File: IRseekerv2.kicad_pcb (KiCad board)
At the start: 2 copper layers, 80 x 80 mm, 49 parts, among them J13 Conn_01x04_Pin, J14 Conn_01x02_Pin, J15 SEL_VOLTAGE, J16 G, J17 G, J18 G, J19 G, J20 Conn_01x02_Pin, J26 Conn_01x02_Pin, J27 Conn_01x02_Pin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

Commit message: BOOT0 pulldown instead of pullup
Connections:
- R3 pad 1: +3.3V -> GND
- SW2 pad 2: GND -> +3.3V
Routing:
- net GND: track 44.2 -> 54.6 mm, vias 26 -> 28
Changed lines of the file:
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@@
       (net 16 "BOOT0") (pinfunction "1") (pintype "passive"))
     (pad "2" thru_hole circle (at 0 4.5 270) (size 2 2) (drill 1.1) (layers "*.Cu" "*.Mask")
-      (net 4 "GND") (pinfunction "2") (pintype "passive"))
+      (net 5 "+3.3V") (pinfunction "2") (pintype "passive"))
     (pad "2" thru_hole circle (at 6.5 4.5 270) (size 2 2) (drill 1.1) (layers "*.Cu" "*.Mask")
-      (net 4 "GND") (pinfunction "2") (pintype "passive"))
+      (net 5 "+3.3V") (pinfunction "2") (pintype "passive"))
     (model "${KICAD6_3DMODEL_DIR}/Button_Switch_THT.3dshapes/SW_PUSH_6mm.wrl"
       (offset (xyz 0 0 0))
@@
       (stroke (width 0.1) (type solid)) (layer "F.Fab"))
     (pad "1" smd roundrect (at -0.825 0) (size 0.8 0.95) (layers "F.Cu" "F.Paste" "F.Mask") (roundrect_rratio 0.25)
-      (net 5 "+3.3V") (pintype "passive"))
+      (net 4 "GND") (pintype "passive"))
     (pad "2" smd roundrect (at 0.825 0) (size 0.8 0.95) (layers "F.Cu" "F.Paste" "F.Mask") (roundrect_rratio 0.25)
       (net 16 "BOOT0") (pintype "passive"))
@@
     (effects (font (size 0.75 0.75) (thickness 0.1875) bold) (justify left bottom mirror))
   )
+  (gr_text "5V" (at 105.89 125.15) (layer "B.SilkS")
+    (effects (font (size 0.75 0.75) (thickness 0.1875) bold) (justify left bottom mirror))
+  )
   (gr_text "TX_3V" (at 119.96 100.614 90) (layer "B.SilkS")
     (effects (font (size 0.75 0.75) (thickness 0.1875) bold) (justify left bottom mirror))
   )
+  (gr_text "GND" (at 108.74 125.2) (layer "B.SilkS")
+    (effects (font (size 0.75 0.75) (thickness 0.1875) bold) (justify left bottom mirror))
+  )
   (gr_text "3V" (at 134.826 109.088 90) (layer "B.SilkS")
     (effects (font (size 0.75 0.75) (thickness 0.1875) bold) (justify left bottom mirror))
@@
     (effects (font (size 0.75 0.75) (thickness 0.1875) bold) (justify left bottom))
   )
-  (gr_text "5V" (at 106.7 123.9 90) (layer "F.SilkS")
+  (gr_text "5V" (at 104.32 125.14) (layer "F.SilkS")
     (effects (font (size 0.75 0.75) (thickness 0.1875) bold) (justify left bottom))
   )
@@
     (effects (font (size 1.5 1.5) (thickness 0.3)))
   )
-  (gr_text "GND" (at 106.65 127.25 90) (layer "F.SilkS")
+  (gr_text "GND" (at 106.27 125.2) (layer "F.SilkS")
     (effects (font (size 0.75 0.75) (thickness 0.1875) bold) (justify left bottom))
   )
@@
   (segment (start 106.335 109.64) (end 106.35 109.655) (width 0.25) (layer "F.Cu") (net 4))
   (segment (start 106.35 109.655) (end 108.35 109.655) (width 0.25) (layer "F.Cu") (net 4))
+  (segment (start 90.265 75.17) (end 89.9 75.17) (width 0.25) (layer "F.Cu") (net 4))
   (segment (start 103.7298 82.3805) (end 105.6525 82.3805) (width 0.25) (layer "F.Cu") (net 4))
+  (segment (start 89.32 82.135) (end 91.03 80.425) (width 0.25) (layer "F.Cu") (net 4))
   (segment (start 103.06 109.64) (end 104.5311 109.64) (width 0.25) (layer "F.Cu") (net 4))
   (segment (start 100.2401 90.5964) (end 101.2964 90.5964) (width 0.25) (layer "F.Cu") (net 4))
   (segment (start 104.5311 109.64) (end 104.5311 109.418) (width 0.25) (layer "F.Cu") (net 4))
+  (segment (start 89.32 82.22) (end 89.32 82.135) (width 0.25) (layer "F.Cu") (net 4))
   (segment (start 111.6919 123.1652) (end 113.48 124.9533) (width 0.25) (layer "F.Cu") (net 4))
   (segment (start 77.395 98.91) (end 77.395 97.74) (width 0.25) (layer "F.Cu") (net 4))
@@
   (segment (start 114.7293 97.8136) (end 113.8814 97.8136) (width 0.25) (layer "F.Cu") (net 4))
   (segment (start 115.7734 73.1094) (end 116.6236 73.1094) (width 0.25) (layer "F.Cu") (net 4))
+  (segment (start 89.9 75.17) (end 88.94 76.13) (width 0.25) (layer "F.Cu") (net 4))
   (segment (start 94.9076 97.3126) (end 95.275 97.68) (width 0.25) (layer "F.Cu") (net 4))
   (segment (start 108.35 109.655) (end 108.36 109.665) (width 0.25) (layer "F.Cu") (net 4))
@@
   (via (at 103.06 100.54) (size 0.8) (drill 0.4) (layers "F.Cu" "B.Cu") (net 4))
   (via (at 103.56 99.54) (size 0.8) (drill 0.4) (layers "F.Cu" "B.Cu") (net 4))
+  (via (at 89.32 82.22) (size 0.8) (drill 0.4) (layers "F.Cu" "B.Cu") (net 4))
   (via (at 102.13 99.5) (size 0.8) (drill 0.4) (layers "F.Cu" "B.Cu") (net 4))
   (via (at 106.23 100.46) (size 0.8) (drill 0.4) (layers "F.Cu" "B.Cu") (net 4))
@@
   (via (at 115.7734 73.1094) (size 0.8) (drill 0.4) (layers "F.Cu" "B.Cu") (net 4))
   (via (at 87.8748 91.9783) (size 0.8) (drill 0.4) (layers "F.Cu" "B.Cu") (net 4))
+  (via (at 88.94 76.13) (size 0.8) (drill 0.4) (layers "F.Cu" "B.Cu") (net 4))
   (via (at 104.92 98.42) (size 0.8) (drill 0.4) (layers "F.Cu" "B.Cu") (net 4))
   (via (at 103.95 100.52) (size 0.8) (drill 0.4) (layers "F.Cu" "B.Cu") (net 4))
   (via (at 100.2401 90.5964) (size 0.8) (drill 0.4) (layers "F.Cu" "B.Cu") (net 4))
   (via (at 92.1279 80.4589) (size 0.8) (drill 0.4) (layers "F.Cu" "B.Cu") (net 4))
+  (segment (start 89.32 76.51) (end 89.32 82.22) (width 0.25) (layer "B.Cu") (net 4))
   (segment (start 93.5333 98.132195) (end 97.400255 101.99915) (width 0.25) (layer "B.Cu") (net 4))
   (segment (start 100.61085 101.99915) (end 102.13 100.48) (width 0.25) (layer "B.Cu") (net 4))
   (segment (start 102.14 99.51) (end 102.13 99.5) (width 3) (layer "B.Cu") (net 4))
   (segment (start 106.23 99.51) (end 102.14 99.51) (width 3) (layer "B.Cu") (net 4))
+  (segment (start 88.94 76.13) (end 89.32 76.51) (width 0.25) (layer "B.Cu") (net 4))
   (segment (start 97.400255 101.99915) (end 100.61085 101.99915) (width 0.25) (layer "B.Cu") (net 4))
   (segment (start 93.5333 97.3126) (end 93.5333 98.132195) (width 0.25) (layer "B.Cu") (net 4))
@@
     (polygon
       (pts
-        (xy 197.75 176.25)
-        (xy -8.75 178)
-        (xy -9.5 18.75)
-        (xy 197.75 18.75)
+        (xy 167.06 153.7)
+        (xy 47.24 152.48)
+        (xy 49.27 48.1)
+        (xy 167.87 47.69)
       )
     )
@@
     (polygon
       (pts
-        (xy 194 -4)
-        (xy 189.5 226.25)
-        (xy 15.75 231.25)
-        (xy 14 -8)
+        (xy 163 55.81)
+        (xy 162.59 150.04)
+        (xy 51.3 148.82)
+        (xy 52.12 55.81)
       )
     )

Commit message: Added label for site and "designed by"
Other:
- board text added: "Designed by Marek Maszay https://github.com/markosko/IRseeker-kicad"
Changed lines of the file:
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@@
   (gr_circle (center 104.09 100.4) (end 144.09 100.4)
     (stroke (width 0.2) (type solid)) (fill none) (layer "Edge.Cuts"))
+  (gr_text "Designed by\nMarek Maszay\nhttps://github.com/markosko/IRseeker-kicad" (at 103.41 98.6) (layer "B.SilkS")
+    (effects (font (size 1 1) (thickness 0.25) bold) (justify bottom mirror))
+  )
   (gr_text "3V" (at 120.04 108.97 90) (layer "B.SilkS")
     (effects (font (size 0.75 0.75) (thickness 0.1875) bold) (justify left bottom mirror))

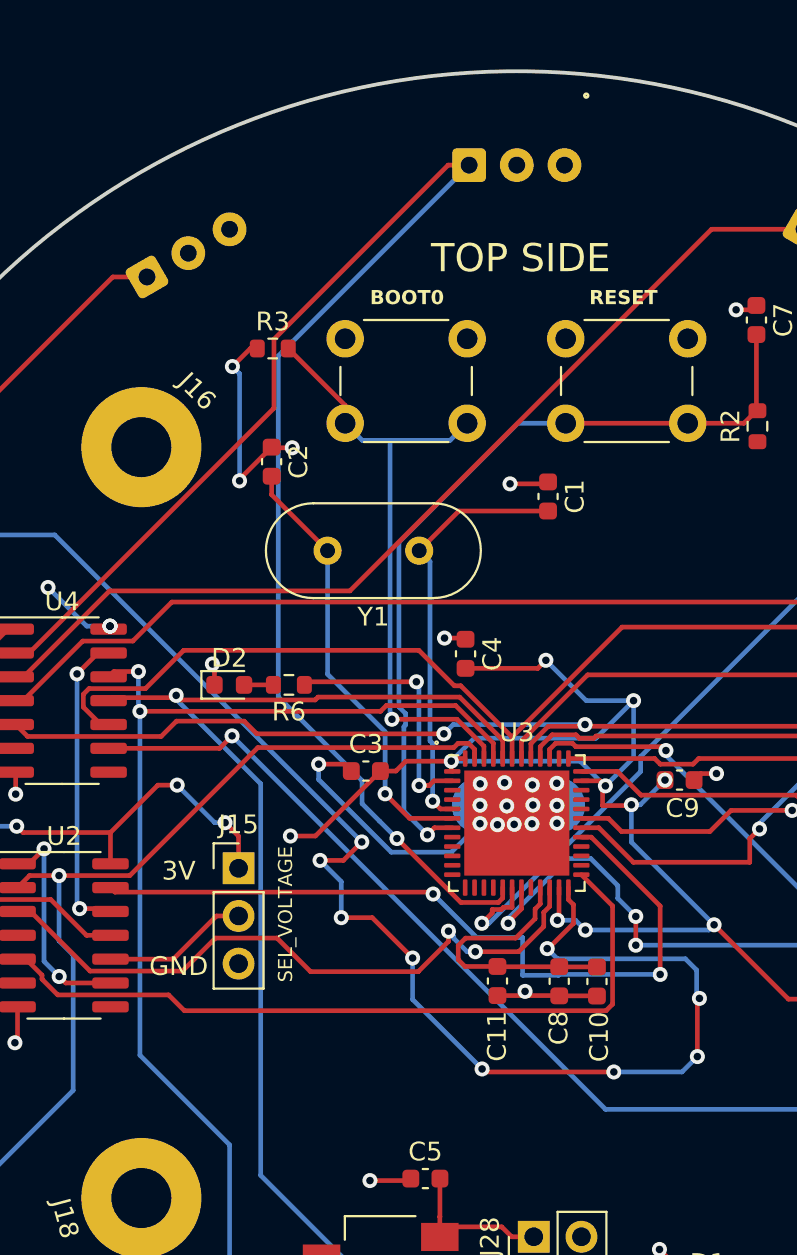
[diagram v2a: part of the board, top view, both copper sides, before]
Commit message: removed SEL_VOlTAGE and added OUTGATE pin out
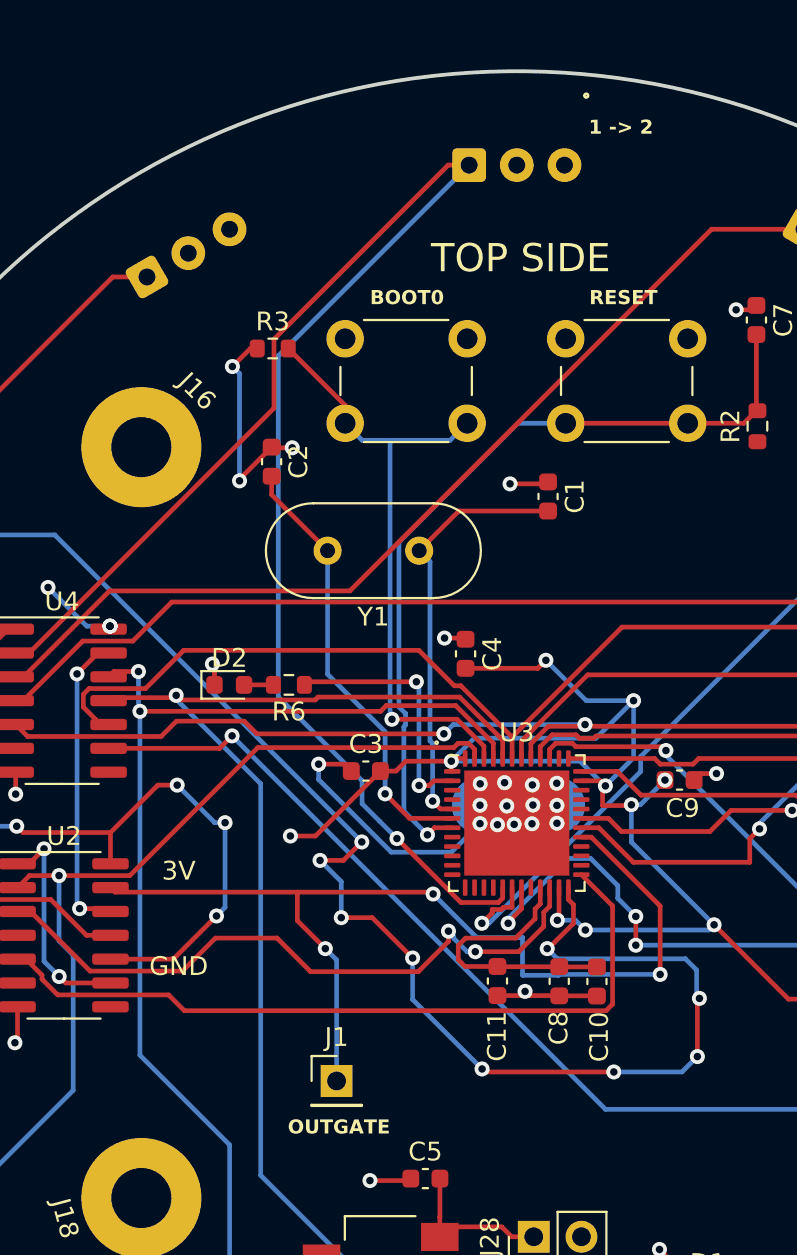
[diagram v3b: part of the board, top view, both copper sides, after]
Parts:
- removed J15: SEL_VOLTAGE, Connector_PinHeader_2.54mm:PinHeader_1x03_P2.54mm_Vertical
- added J1: Conn_01x01_Pin, Connector_PinHeader_2.54mm:PinHeader_1x01_P2.54mm_Vertical, F.Cu at (94.5, 114.2)
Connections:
- U2 pad 10: Net-(J15-Pin_2) -> +3.3V
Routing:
- net OUT_GATE: track 41.8 -> 52.7 mm, vias 2 -> 3
- net +3.3V: track 130.5 -> 139.6 mm, vias 19 -> 20
- net Net-(J15-Pin_2): track 7.78 -> 0.00 mm
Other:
- board text added: "1 -> 2"
- board text added: "2 <- 1"
- board text added: "BOTTOM SIDE"
- board text added: "OUTGATE"

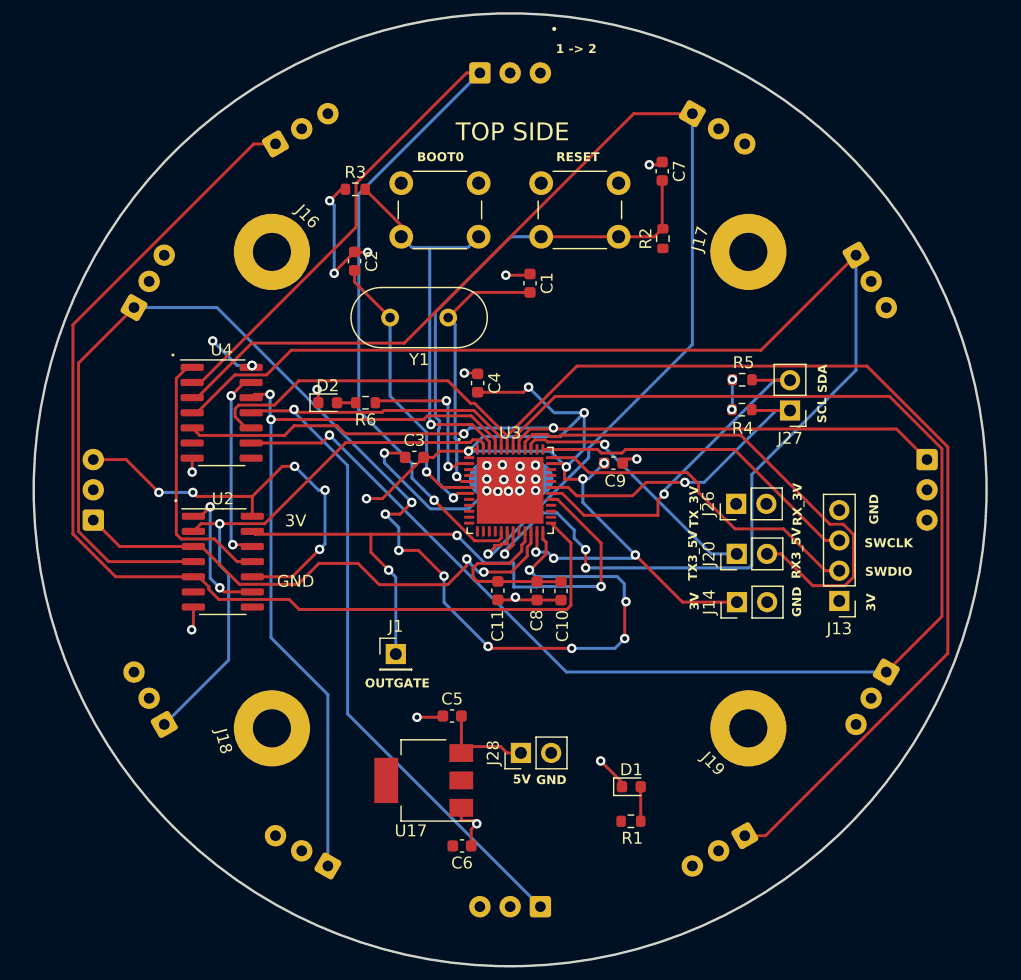
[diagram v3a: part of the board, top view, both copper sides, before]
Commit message: change crystal to smd version
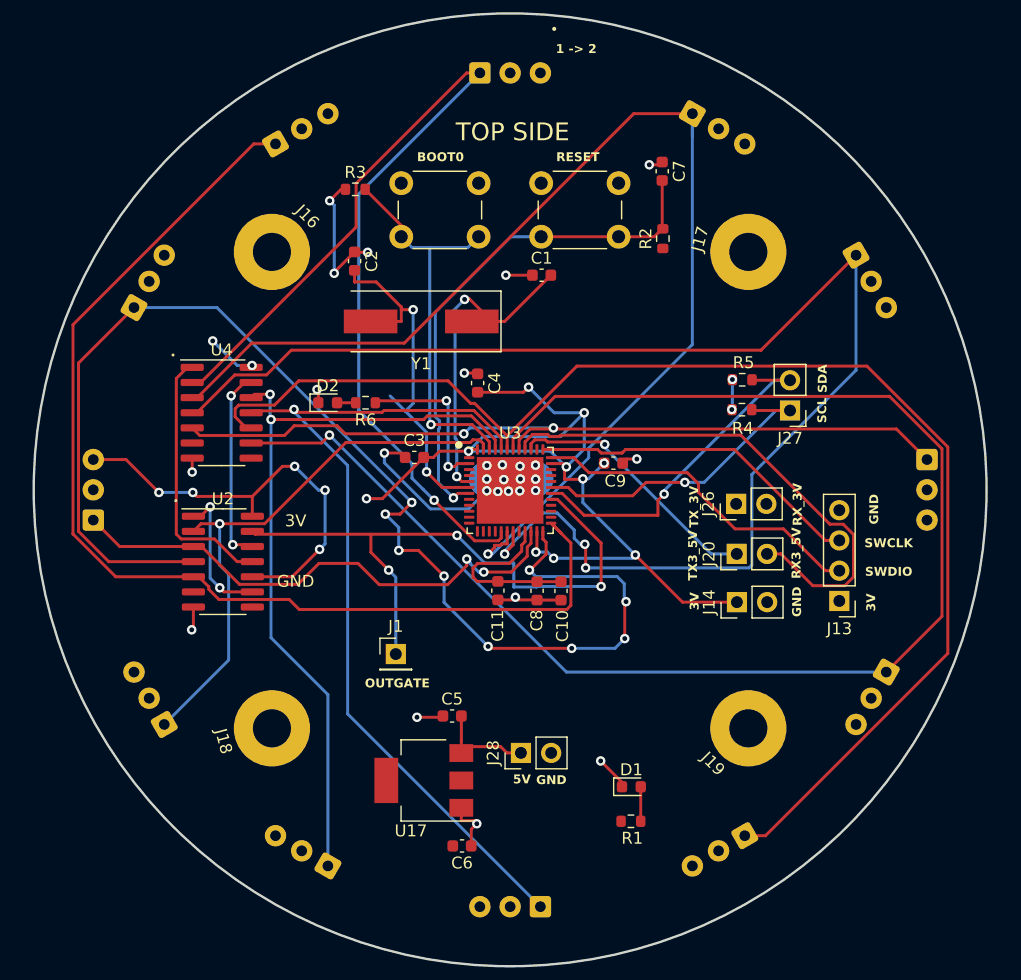
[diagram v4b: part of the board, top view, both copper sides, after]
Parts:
- Y1: footprint Crystal:Crystal_HC49-4H_Vertical -> Crystal:Crystal_SMD_HC49-SD
- moved Y1 2.29 mm to (96.6, 86.3)
- moved C1 1.19 mm to (106.7, 82.4), turned to 0 degrees
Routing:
- net Net-(U3-PF1): track 23.5 -> 32.8 mm, vias 1 -> 2
- net Net-(U3-PF0): track 22.6 -> 26.8 mm, vias 1 -> 2
- net I2: track 99.3 -> 101.2 mm
- net I12: track 93.2 -> 94.3 mm
- net I3: track 119.1 -> 119.9 mm
- net +3.3V: vias 20 -> 19

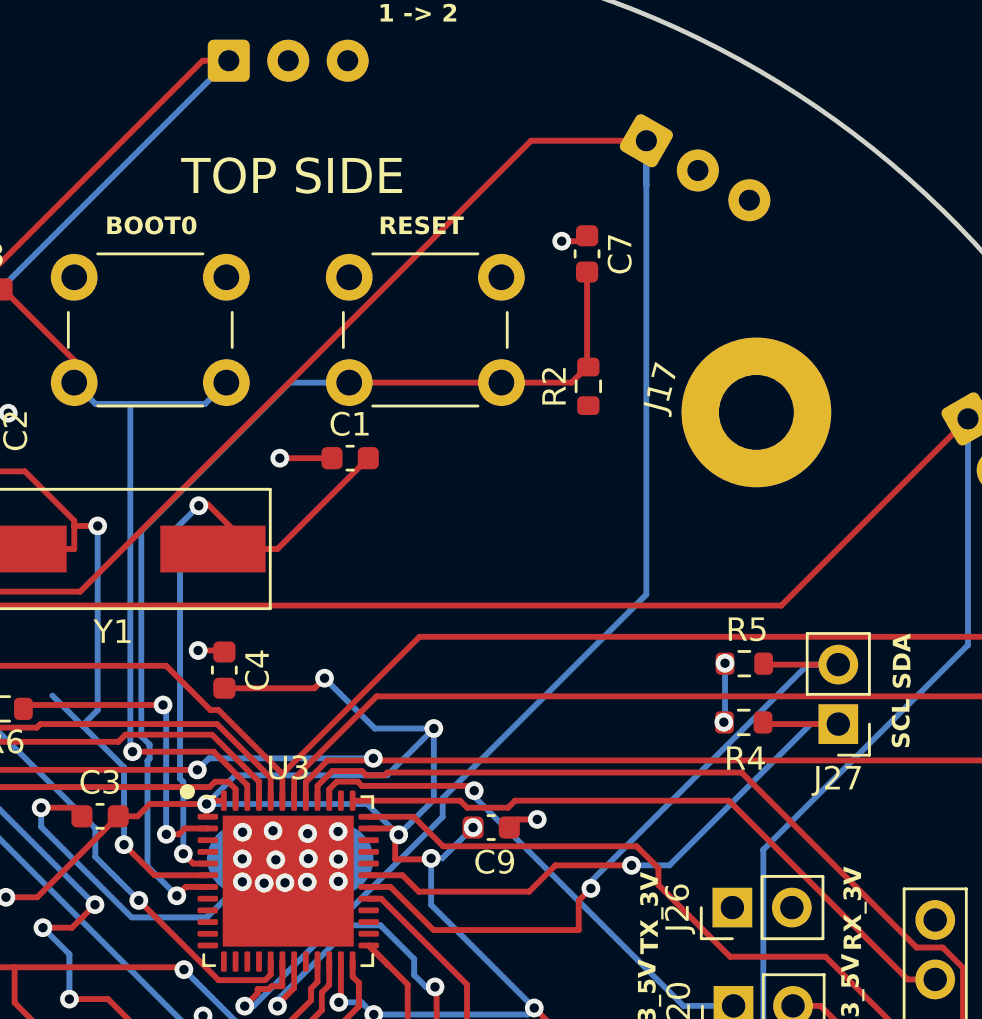
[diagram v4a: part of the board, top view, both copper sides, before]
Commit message: STOP_COMM pin, solder pads for resistors on I2C lines
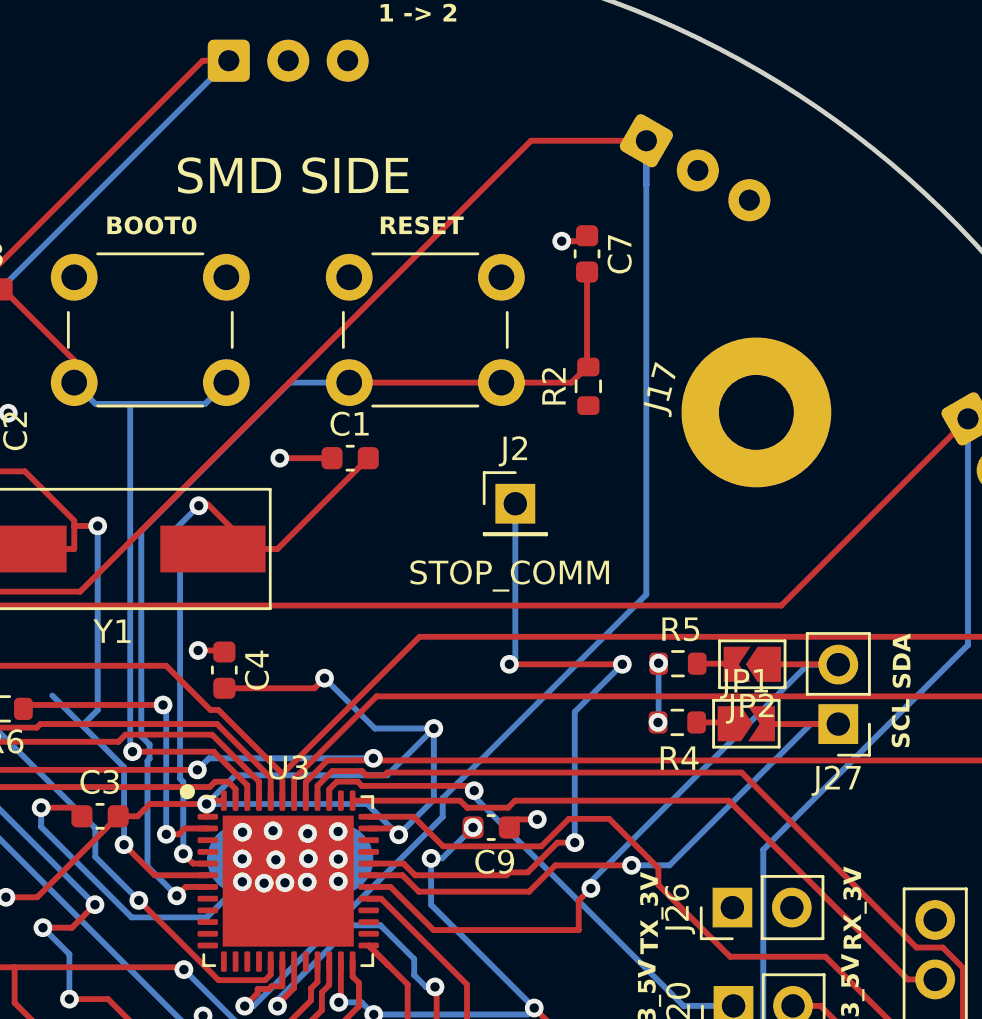
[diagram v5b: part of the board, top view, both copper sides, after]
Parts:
- added G***: LOGO, LOGO, B.Cu at (104.1, 113.0)
- added J2: Conn_01x01_Pin, Connector_PinHeader_2.54mm:PinHeader_1x01_P2.54mm_Vertical, F.Cu at (113.8, 84.3)
- added JP1: SolderJumper_2_Open, Jumper:SolderJumper-2_P1.3mm_Open_TrianglePad1.0x1.5mm, F.Cu at (123.7, 93.7)
- added JP2: SolderJumper_2_Open, Jumper:SolderJumper-2_P1.3mm_Open_TrianglePad1.0x1.5mm, F.Cu at (123.9, 91.2)
- R4, R5: value 4.7kR -> 82kR
- moved R4 2.84 mm to (120.7, 93.7)
- moved R5 2.84 mm to (120.7, 91.2)
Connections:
- R4 pad 2: SCL -> Net-(JP1-A)
- R5 pad 1: SDA -> Net-(JP2-B)
- U3 pad 32: unconnected-(U3-PA10-Pad32) -> DISABLE_COMM
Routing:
- net DISABLE_COMM: track 0.00 -> 29.8 mm, vias 0 -> 3
- net +3.3V: track 139.6 -> 137.1 mm
- net Net-(JP2-B): track 0.00 -> 1.64 mm
- net Net-(JP1-A): track 0.00 -> 1.42 mm
- net SWDIO: track 28.6 -> 29.5 mm
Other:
- board text added: "SENSOR SIDE"
- board text added: "SMD SIDE"
- board text added: "STOP_COMM"
- board text added: "Sponsored by"
- board text removed: "BOTTOM SIDE"
- board text removed: "TOP SIDE"
